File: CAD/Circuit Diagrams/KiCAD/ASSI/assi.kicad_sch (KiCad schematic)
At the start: 23 parts, among them SW2 SW_Push, SW3 SW_Push

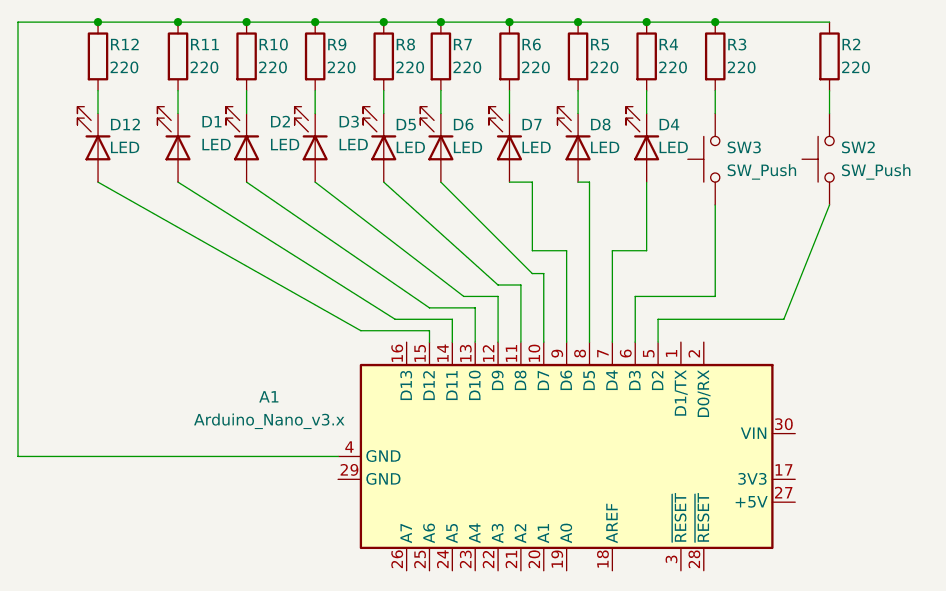
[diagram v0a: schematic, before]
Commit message: Makes the ASSI PCB routing better and puts it somewhere that makes more sense
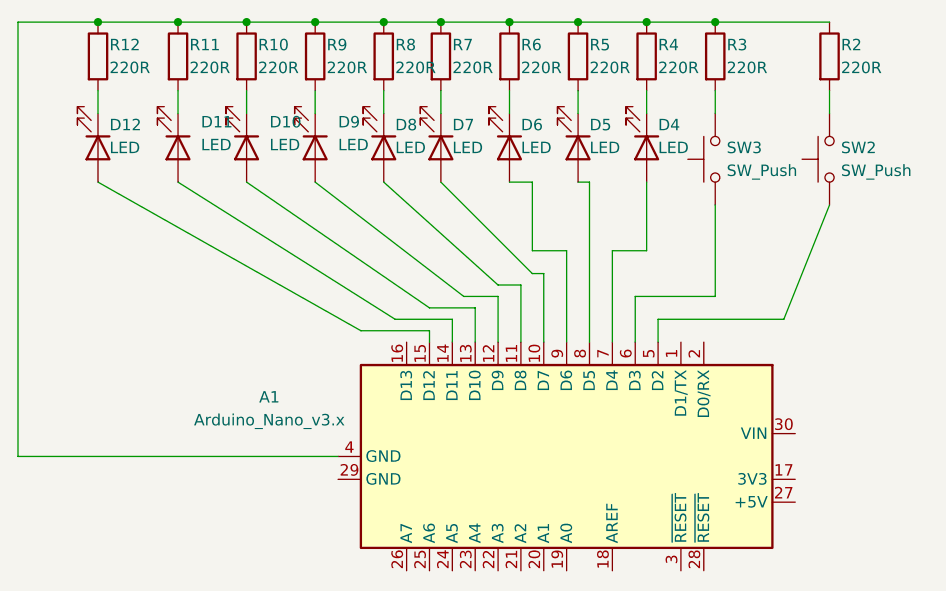
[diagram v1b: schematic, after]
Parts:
- R10, R11, R12, R2, R3, R4, R5, R6, R7, R8, R9: value 220 -> 220R
- renumbered D2 to D10, D1 to D11, D8 to D5, D7 to D6, D6 to D7, D5 to D8, D3 to D9
